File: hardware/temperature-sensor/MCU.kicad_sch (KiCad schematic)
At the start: 43 parts, among them J4 ARM-JTAG-SWD, Q2 DMN3404L, Q3 DMN3404L, Q4 DMN3404L, U1 STM32F407V_E-G_Tx, U4 AT24C512C, Y1 CX2016FB25000C0FZZH1

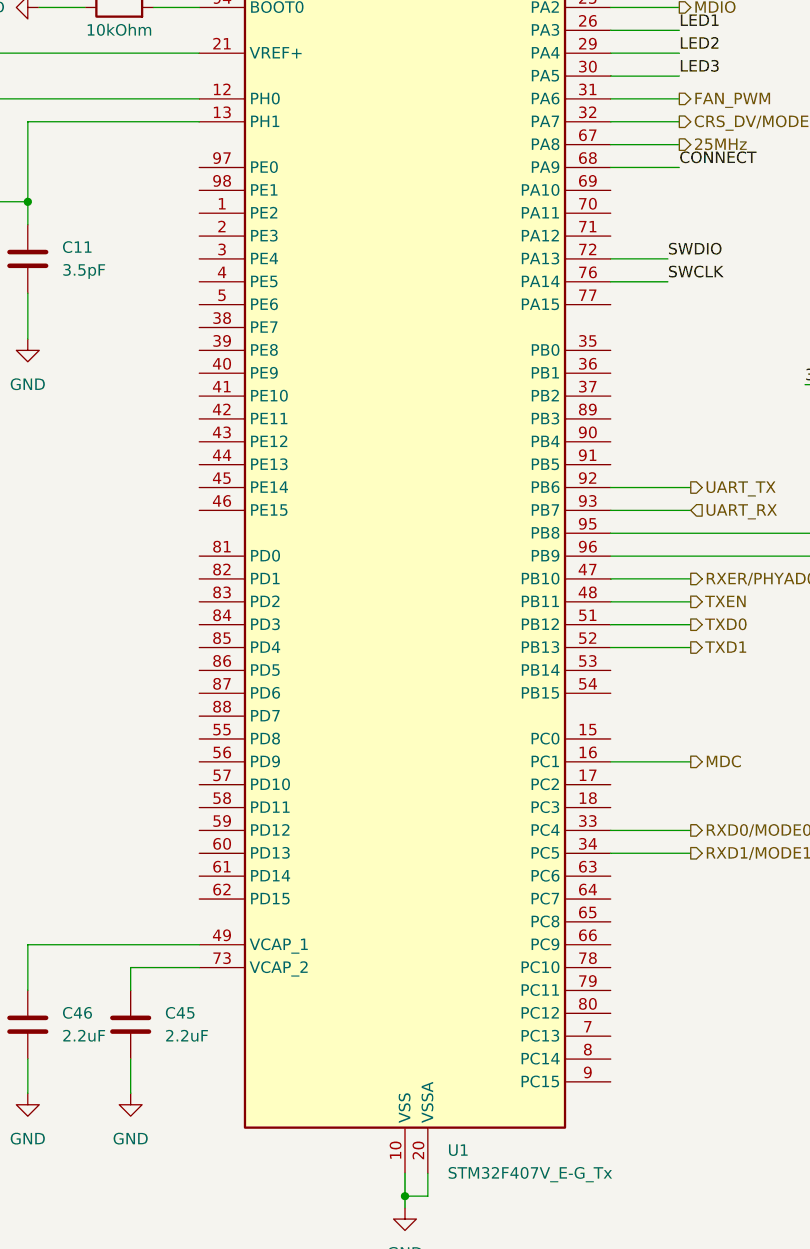
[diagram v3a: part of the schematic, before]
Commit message: finish placement
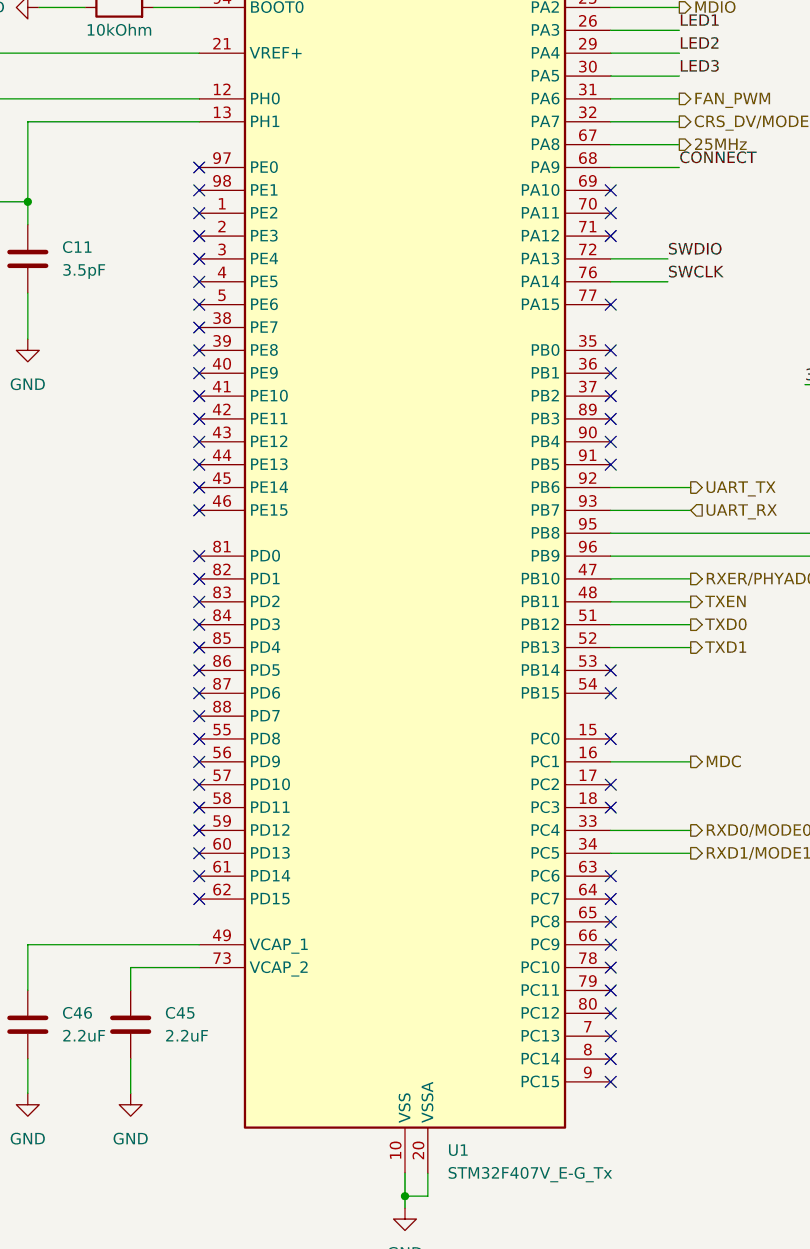
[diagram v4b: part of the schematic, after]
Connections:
- no-connect marks 3 -> 60
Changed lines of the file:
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@@
+	)
+	(no_connect
+		(at 83.82 148.59)
+	)
+	(no_connect
+		(at 83.82 140.97)
+	)
+	(no_connect
+		(at 129.54 146.05)
 	)
 	(no_connect
@@
 	)
 	(no_connect
+		(at 129.54 176.53)
+	)
+	(no_connect
+		(at 83.82 105.41)
+	)
+	(no_connect
+		(at 83.82 133.35)
+	)
+	(no_connect
+		(at 83.82 153.67)
+	)
+	(no_connect
+		(at 129.54 80.01)
+	)
+	(no_connect
+		(at 83.82 87.63)
+	)
+	(no_connect
+		(at 129.54 171.45)
+	)
+	(no_connect
+		(at 83.82 125.73)
+	)
+	(no_connect
+		(at 129.54 156.21)
+	)
+	(no_connect
+		(at 83.82 130.81)
+	)
+	(no_connect
+		(at 129.54 130.81)
+	)
+	(no_connect
+		(at 129.54 161.29)
+	)
+	(no_connect
+		(at 83.82 138.43)
+	)
+	(no_connect
+		(at 129.54 173.99)
+	)
+	(no_connect
+		(at 83.82 107.95)
+	)
+	(no_connect
+		(at 83.82 95.25)
+	)
+	(no_connect
+		(at 83.82 113.03)
+	)
+	(no_connect
+		(at 129.54 163.83)
+	)
+	(no_connect
+		(at 83.82 156.21)
+	)
+	(no_connect
+		(at 129.54 102.87)
+	)
+	(no_connect
+		(at 83.82 151.13)
+	)
+	(no_connect
+		(at 129.54 133.35)
+	)
+	(no_connect
+		(at 129.54 158.75)
+	)
+	(no_connect
+		(at 129.54 82.55)
+	)
+	(no_connect
+		(at 83.82 74.93)
+	)
+	(no_connect
+		(at 83.82 120.65)
+	)
+	(no_connect
+		(at 129.54 107.95)
+	)
+	(no_connect
+		(at 83.82 80.01)
+	)
+	(no_connect
+		(at 129.54 153.67)
+	)
+	(no_connect
+		(at 83.82 143.51)
+	)
+	(no_connect
+		(at 129.54 90.17)
+	)
+	(no_connect
+		(at 83.82 123.19)
+	)
+	(no_connect
+		(at 129.54 97.79)
+	)
+	(no_connect
+		(at 83.82 128.27)
+	)
+	(no_connect
+		(at 83.82 92.71)
+	)
+	(no_connect
+		(at 83.82 77.47)
+	)
+	(no_connect
+		(at 129.54 143.51)
+	)
+	(no_connect
+		(at 83.82 146.05)
+	)
+	(no_connect
+		(at 83.82 82.55)
+	)
+	(no_connect
+		(at 83.82 118.11)
+	)
+	(no_connect
+		(at 129.54 95.25)
+	)
+	(no_connect
+		(at 129.54 138.43)
+	)
+	(no_connect
+		(at 129.54 166.37)
+	)
+	(no_connect
+		(at 83.82 110.49)
+	)
+	(no_connect
 		(at 184.15 36.83)
+	)
+	(no_connect
+		(at 83.82 100.33)
+	)
+	(no_connect
+		(at 129.54 168.91)
+	)
+	(no_connect
+		(at 129.54 77.47)
 	)
 	(no_connect
 		(at 209.55 34.29)
 	)
+	(no_connect
+		(at 83.82 85.09)
+	)
+	(no_connect
+		(at 83.82 97.79)
+	)
+	(no_connect
+		(at 129.54 105.41)
+	)
+	(no_connect
+		(at 83.82 102.87)
+	)
+	(no_connect
+		(at 83.82 90.17)
+	)
+	(no_connect
+		(at 83.82 135.89)
+	)
+	(no_connect
+		(at 129.54 100.33)
+	)
 	(wire

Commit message: update symbols from library
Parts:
- U1: Mouser Part No 511-STM32F407VGT6TR -> (none); Mouser Part Number (none) -> 511-STM32F407VGT6
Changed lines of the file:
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@@
 			)
 		)
-		(property "Mouser Part No" "511-STM32F407VGT6TR"
+		(property "Mouser Part Number" "511-STM32F407VGT6"
 			(at 106.68 115.57 0)
 			(effects
